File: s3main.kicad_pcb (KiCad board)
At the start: 2 copper layers, 75 x 60 mm, 151 parts, among them J1 TRACK, J2 IDC, J3 POWER, J4 USB_C_Receptacle_USB2.0_16P, J5 ZUSI, Q1 QS6K21, Q10 BSS138, Q2 BC847BDW1, Q3 SiS4634LDN, Q4 SiS4634LDN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

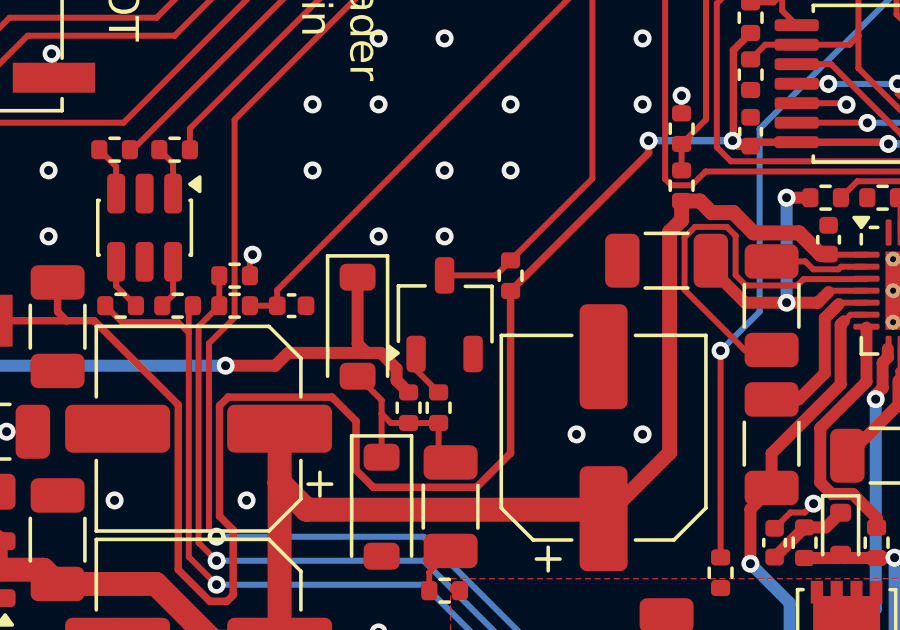
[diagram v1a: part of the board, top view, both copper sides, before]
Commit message: chore: use consistent SOT-23-3 footprint
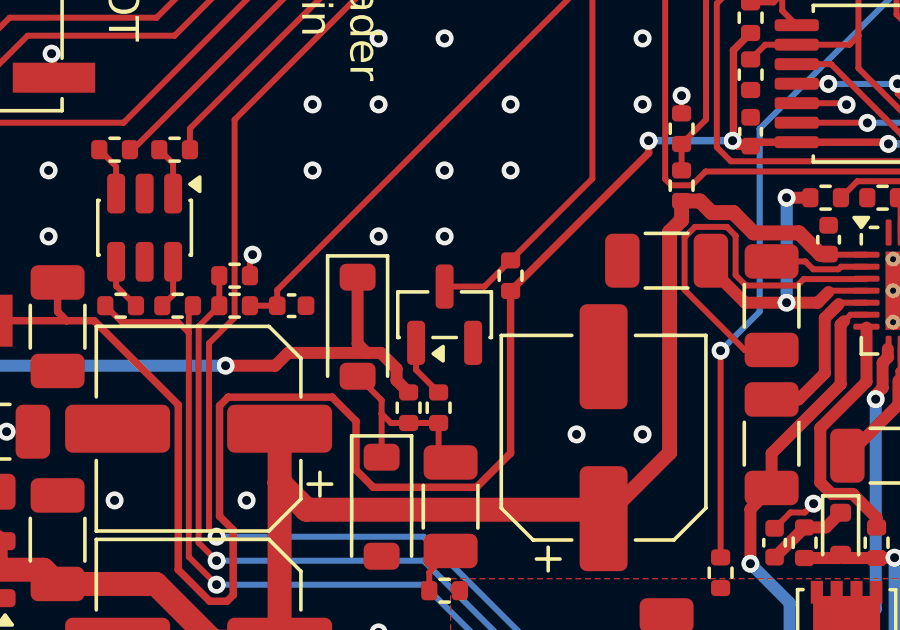
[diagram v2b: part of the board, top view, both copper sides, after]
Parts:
- Q10: footprint Package_TO_SOT_SMD:TSOT-23 -> Package_TO_SOT_SMD:SOT-23
